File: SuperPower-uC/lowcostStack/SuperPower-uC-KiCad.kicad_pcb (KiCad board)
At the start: 4 copper layers, 92.2 x 45.2 mm, 105 parts, among them J1 Battery connector, J10 External NTC, J11 DNP, J2 Thermistor, J3 USB_B_Micro, J4 Solar in, J5 Conn_01x14_Female, J6 Conn_01x14_Female, J7 DNP, J8 regulator board, J9 MCU board, Q1 2N7002, Q2 2N7002, Q3 S8050, Q4 S8050, Q5 AO3401A, Q6 AO3401A, Q7 2N7002, Q8 2N7002, Q9 AO3401A, SW1 DNP, SW2 DNP, U1 AP9101CK6-ADTRG1, U10 FP6291LR, U11 ME6210A33P, U12 ME6210A33P, U13 ESP32-WROOM32, U14 W25Q32JVSS, U15 IP4220CZ6, U2 FS8205A, U3 LC709203FQH, U4 TP4056, U5 CH340G, U6 AMS1117-3.3, U7 PCF8563T, U8 XC6206P332MR, U9 TCA6408A, Y1 12MHZ, Y2 32.768KHz

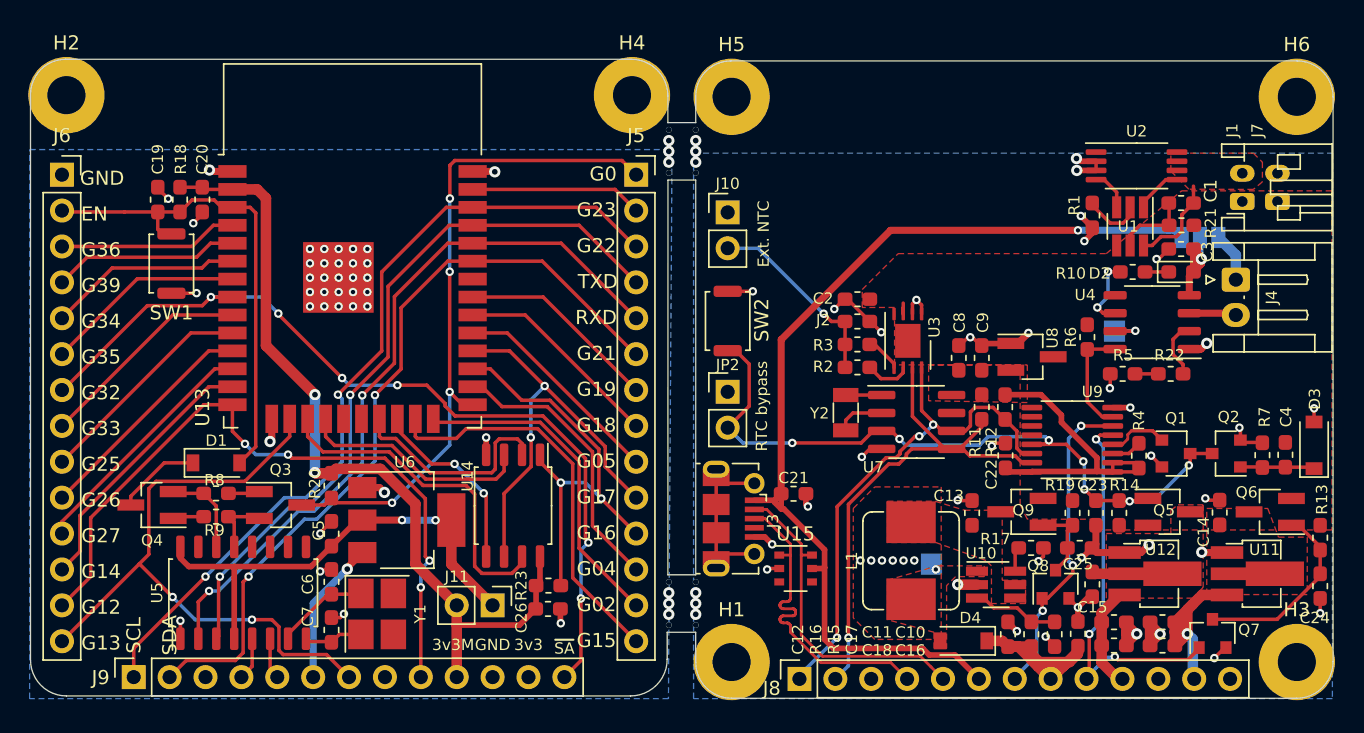
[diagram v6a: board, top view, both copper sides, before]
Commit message: rerouted psram track, added silk function groups...
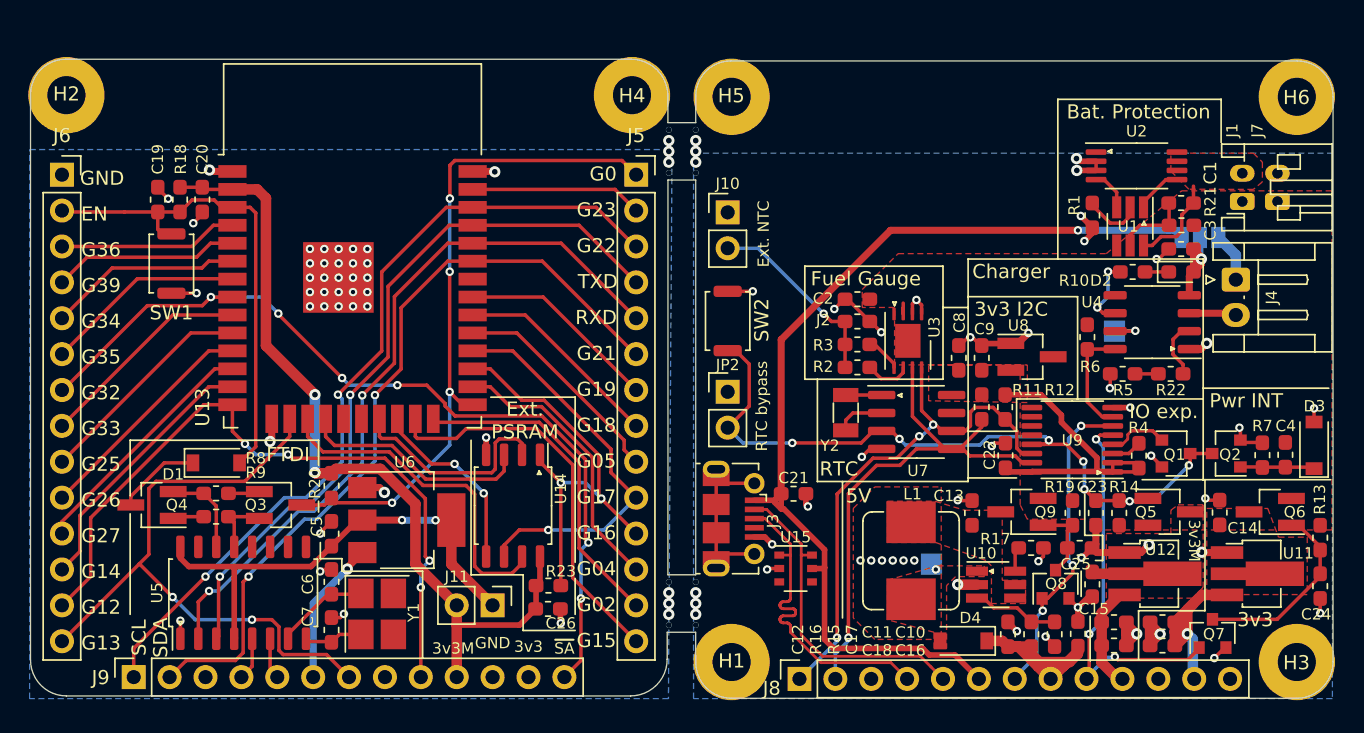
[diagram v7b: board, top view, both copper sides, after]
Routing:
- net /MCU Module/IO17: track 30.0 -> 28.4 mm, vias 2 -> 1
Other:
- board text added: "3v3 I2C"
- board text added: "Bat. Protection"
- board text added: "Charger"
- board text added: "Ext. PSRAM"
- board text added: "FTDI"
- board text added: "Fuel Gauge"
- board text added: "IO exp."
- board text added: "Pwr INT"
- board text added: "RTC"

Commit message: swapped mounting holes, fixed overlapping silk and changed board name
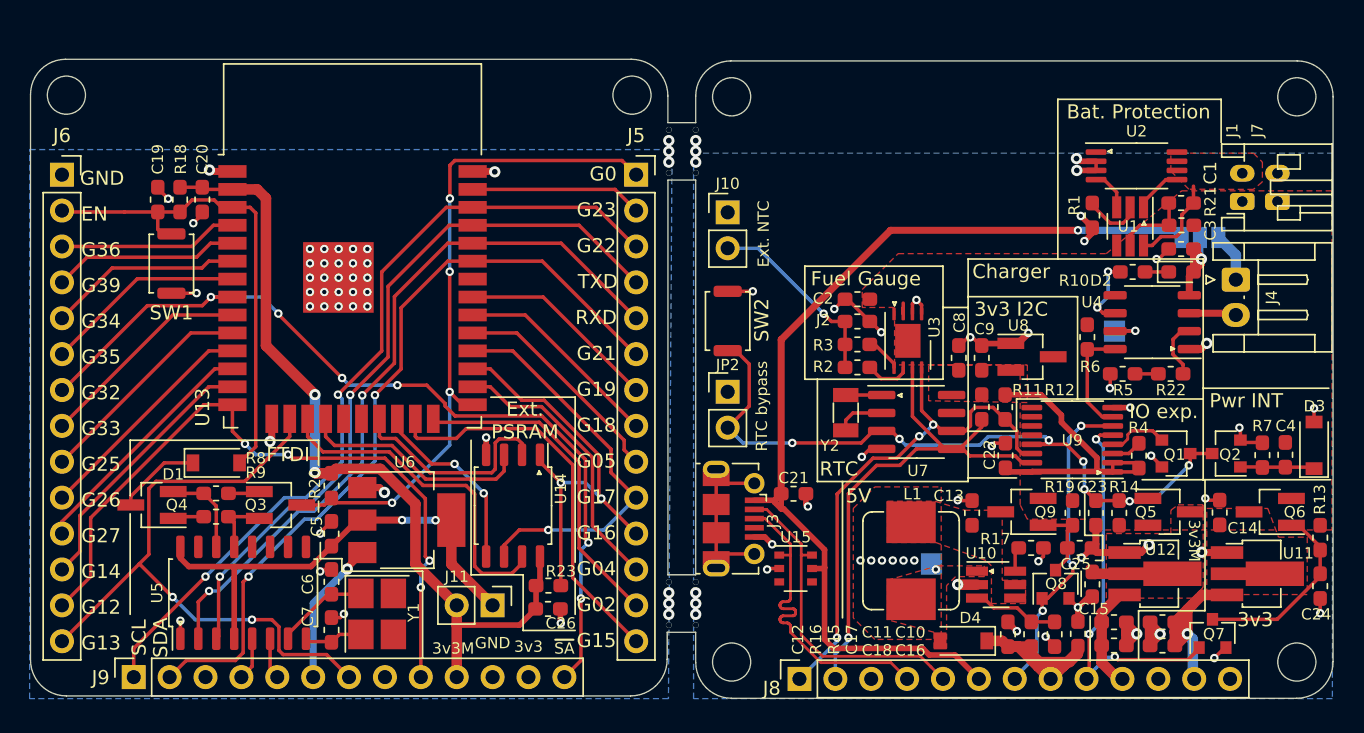
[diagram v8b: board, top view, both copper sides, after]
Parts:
- H1, H2, H3, H4, H5, H6: footprint MountingHole:MountingHole_2.7mm_M2.5_Pad -> MountingHole:MountingHole_2.7mm_M2.5_ISO7380
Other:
- board text added: "ESP32"
- board text added: "v1.00 (2021-02)"
- board text removed: "v1.00 (2021-01)"
